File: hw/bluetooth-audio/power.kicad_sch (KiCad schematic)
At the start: 25 parts, among them J1 Conn_02x02_Odd_Even, J2 Conn_02x01, U2 TPS562200, U3 LD1086DT33TR

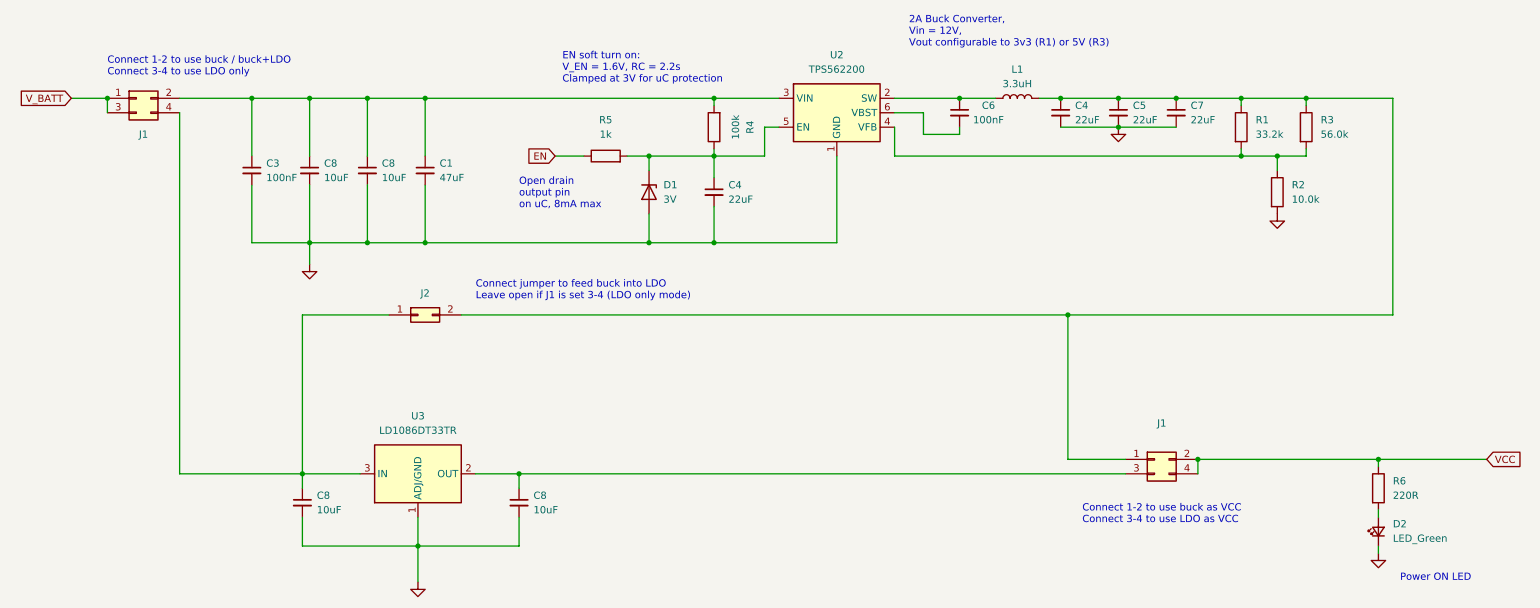
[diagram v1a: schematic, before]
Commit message: Completed design with ESP32D0WD-v3, and JLC production files. High production cost due to req of PCBA standard, due to ESP32 pin pitch.
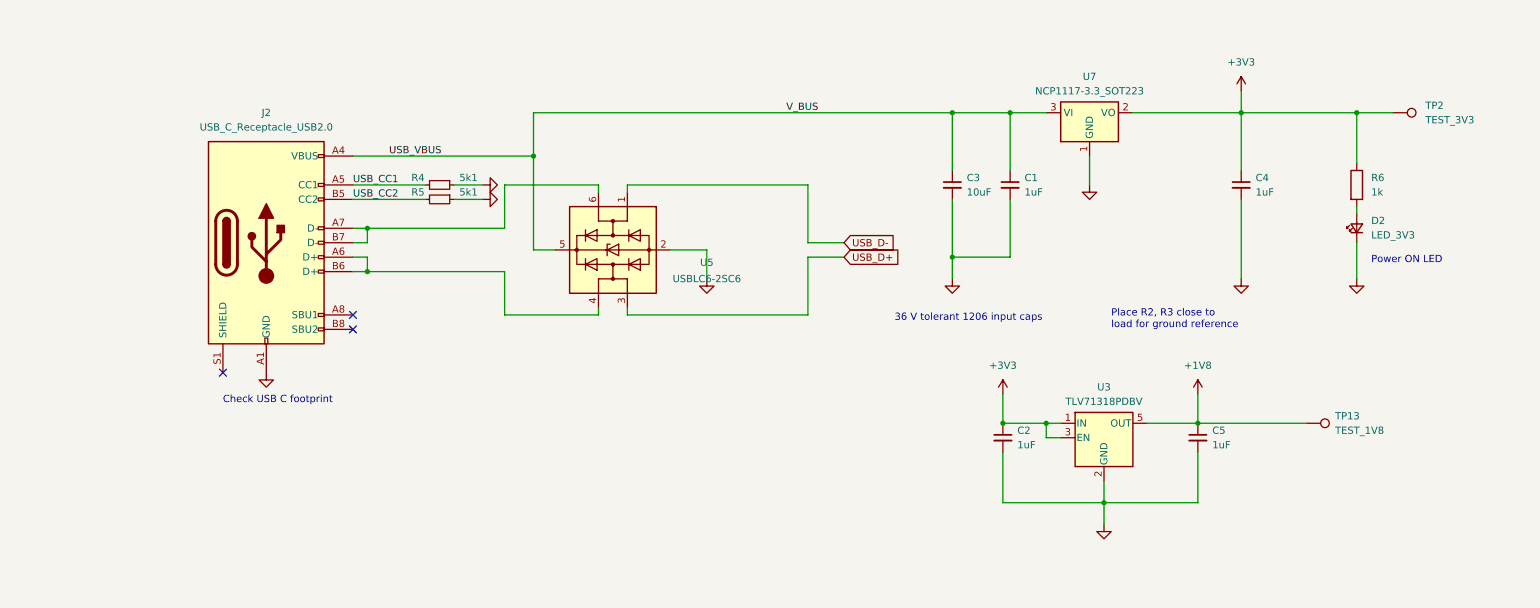
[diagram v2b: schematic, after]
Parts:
- removed C3, C6: 100nF, Capacitor_SMD:C_0603_1608Metric, symbol Device:C_Small
- removed C4 (x2), C7: 22uF, Capacitor_SMD:C_0805_2012Metric, symbol Device:C_Small
- removed C8 (x3): 10uF, Capacitor_SMD:C_1206_3216Metric, symbol Device:C_Small
- removed D1: 3V, Diode_SMD:D_SOD-523, symbol Device:D_Zener
- removed J1 (x2): Conn_02x02_Odd_Even, symbol Connector_Generic:Conn_02x02_Odd_Even
- removed J2: Conn_02x01, symbol Connector_Generic:Conn_02x01
- removed L1: 3.3uH, Inductor_SMD:L_10.4x10.4_H4.8, symbol Device:L
- removed R1: 33.2k, Resistor_SMD:R_0603_1608Metric, symbol Device:R
- removed R2: 10.0k, Resistor_SMD:R_0603_1608Metric, symbol Device:R
- removed R3: 56.0k, Resistor_SMD:R_0603_1608Metric, symbol Device:R
- removed R4: 100k, Resistor_SMD:R_0603_1608Metric, symbol Device:R
- removed R5: 1k, Resistor_SMD:R_0603_1608Metric, symbol Device:R
- removed U2: TPS562200, Package_TO_SOT_SMD:SOT-23-6, symbol Regulator_Switching:TPS562200
- removed U3: LD1086DT33TR, Package_TO_SOT_SMD:TO-252-2, symbol Regulator_Linear:LD1086DT33TR
- added C2, C4: 1uF, Capacitor_SMD:C_0603_1608Metric, symbol Device:C_Small
- added J2: USB_C_Receptacle_USB2.0, Connector_USB:USB_C_Receptacle_GCT_USB4110, symbol Connector:USB_C_Receptacle_USB2.0
- added R4, R5: 5k1, Resistor_SMD:R_0402_1005Metric, symbol Device:R_Small
- added TP13: TEST_1V8, TestPoint:TestPoint_Pad_D1.0mm, symbol Connector:TestPoint
- added TP2: TEST_3V3, TestPoint:TestPoint_Pad_D1.0mm, symbol Connector:TestPoint
- added U3: TLV71318PDBV, Package_TO_SOT_SMD:SOT-23-5, symbol Regulator_Linear:TLV71318PDBV
- added U5: USBLC6-2SC6, Package_TO_SOT_SMD:SOT-23-6, symbol Power_Protection:USBLC6-2SC6
- added U7: NCP1117-3.3_SOT223, Package_TO_SOT_SMD:SOT-223-3_TabPin2, symbol Regulator_Linear:NCP1117-3.3_SOT223
- C1: value 47uF -> 1uF; footprint Capacitor_SMD:C_1210_3225Metric -> Capacitor_SMD:C_1206_3216Metric; Supplier Part Number C6120019 -> C1849
- C5: value 22uF -> 1uF; footprint Capacitor_SMD:C_0805_2012Metric -> Capacitor_SMD:C_0603_1608Metric; Dielectric X7R -> (none); Notes Buck output capacitor -> (none); Supplier Part Number C23692981 -> C1849; Tolerance 20% -> (none)
- D2: value LED_Green -> LED_3V3; footprint LED_SMD:LED_0603_1608Metric -> LED_SMD:LED_0805_2012Metric; Supplier Part Number C5123548 -> C2297
- R6: value 220R -> 1k; footprint (none) -> Resistor_SMD:R_0402_1005Metric
- renumbered C8 to C3
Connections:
- net GND: now also C2.2, C4.2, J2.A1 (GND), J2.A12 (GND), J2.B1 (GND), J2.B12 (GND), R4.1, R5.1, U3.2 (GND), U5.2 (GND), U7.1 (GND)
- net +1V8: now reaches C5.1
- net +1V8: now also TP13.1, U3.5 (OUT)
- net USB_VBUS: now reaches C1.1, C3.1
- net USB_VBUS: now also J2.A4 (VBUS), J2.A9 (VBUS), J2.B4 (VBUS), J2.B9 (VBUS), U5.5 (VBUS), U7.3 (VI)
- net VCC renamed +3V3
- net +3V3: now also C2.1, C4.1, TP2.1, U3.1 (IN), U3.3 (EN), U7.2 (VO)
- new net: J2.A6 (D+), J2.B6 (D+), U5.4 (I/O2)
- new net: J2.A7 (D-), J2.B7 (D-), U5.6 (I/O1)
- new net USB_CC1: J2.A5 (CC1), R4.2
- new net USB_CC2: J2.B5 (CC2), R5.2
- new net USB_D+: U5.3 (I/O2)
- new net USB_D-: U5.1 (I/O1)
- no-connect marks 0 -> 3
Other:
- note added: "36 V tolerant 1206 input caps"
- note added: "Check USB C footprint"
- note added: "Place R2, R3 close to load for ground reference"
- note removed: "2A Buck Converter, Vin = 12V, Vout configurable to 3v3 (R1) or 5V (R3)"
- note removed: "Connect 1-2 to use buck / buck+LDO Connect 3-4 to use LDO only"
- note removed: "Connect 1-2 to use buck as VCC Connect 3-4 to use LDO as VCC"
- note removed: "Connect jumper to feed buck into LDO Leave open if J1 is set 3-4 (LDO only mode)"
- note removed: "EN soft turn on: V_EN = 1.6V, RC = 2.2s Clamped at 3V for uC protection"
- note removed: "Open drain output pin on uC, 8mA max"
- moved on the sheet: C3, D2, R6
